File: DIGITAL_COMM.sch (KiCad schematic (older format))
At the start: 4 parts, among them U5 MCP3004, U6 TC77

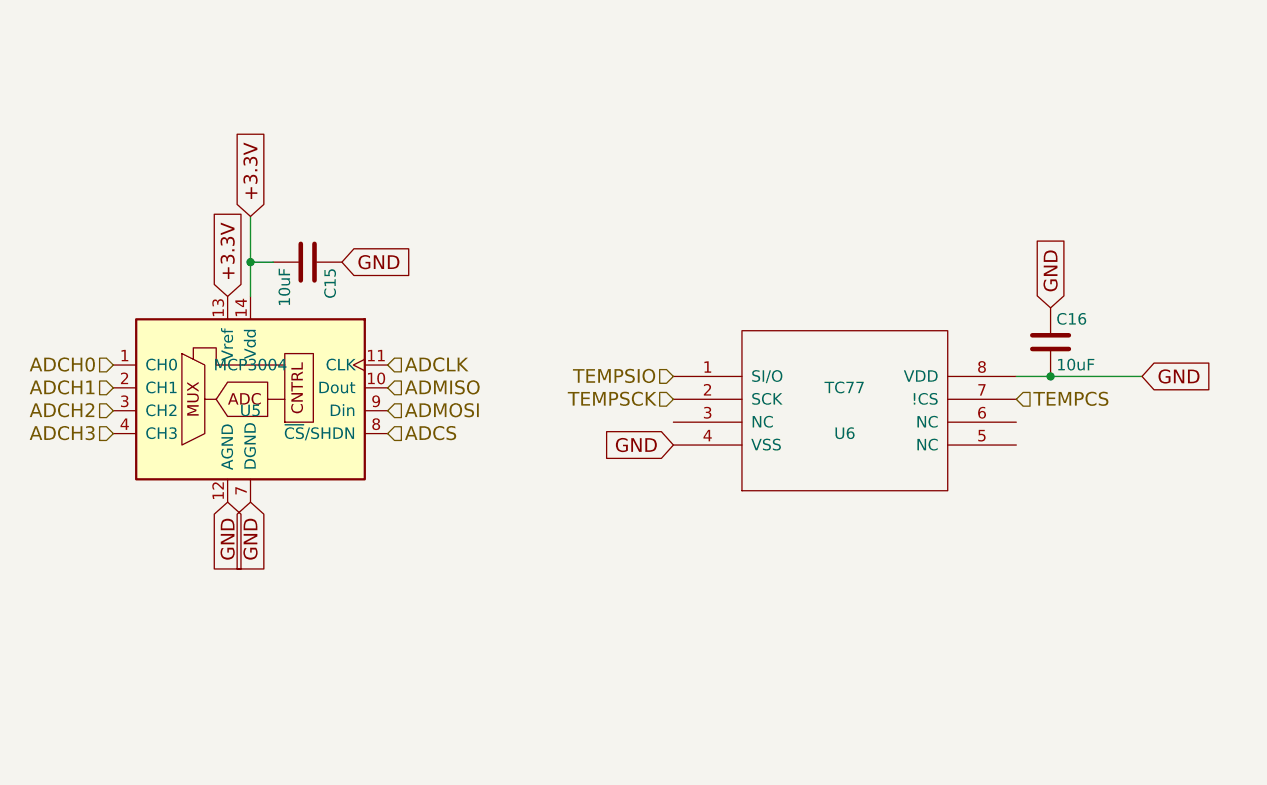
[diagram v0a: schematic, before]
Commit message: all components verified, pcb design required
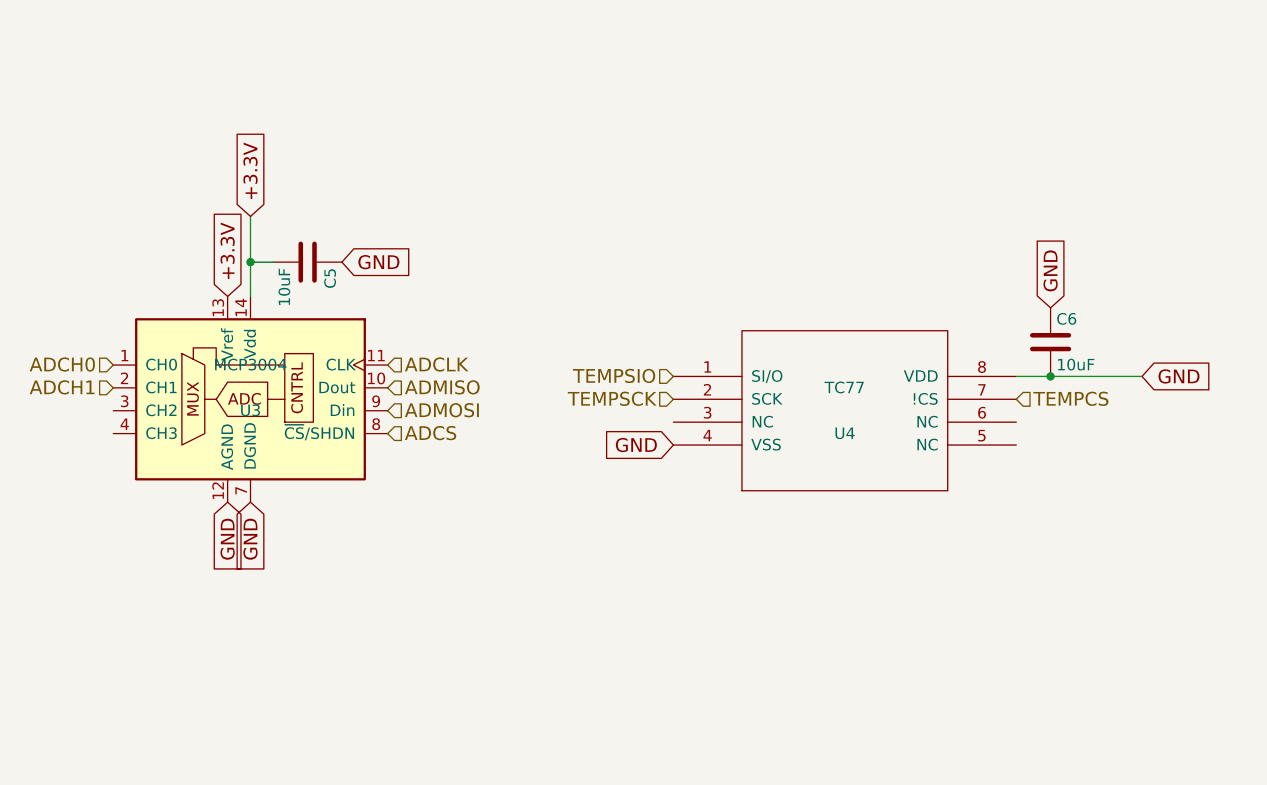
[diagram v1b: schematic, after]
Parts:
- renumbered C15 to C5, C16 to C6, U5 to U3, U6 to U4
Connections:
- net ADCH2: no longer names the net of U3.3 (CH2)
- net ADCH3: no longer names the net of U3.4 (CH3)
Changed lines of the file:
@@
 $EndDescr
 $Comp
-L MCP3004 U5
+L MCP3004 U3
 U 1 1 561B93E7
 P 3550 2600
-F 0 "U5" H 3550 2500 50  0000 C CNN
+F 0 "U3" H 3550 2500 50  0000 C CNN
 F 1 "MCP3004" H 3550 2700 50  0000 C CNN
 F 2 "Housings_SOIC:SOIC-14_3.9x8.7mm_Pitch1.27mm" H 3550 2600 50  0001 C CNN
@@
 $EndComp
 $Comp
-L TC77 U6
+L TC77 U4
 U 1 1 561B943C
 P 6150 2700
-F 0 "U6" H 6150 2600 50  0000 C CNN
+F 0 "U4" H 6150 2600 50  0000 C CNN
 F 1 "TC77" H 6150 2800 50  0000 C CNN
 F 2 "Housings_SOIC:SOIC-8_3.9x4.9mm_Pitch1.27mm" H 6150 2700 50  0001 C CNN
@@
 $EndComp
 $Comp
-L C C16
+L C C6
 U 1 1 561C1F39
 P 7050 2400
-F 0 "C16" H 7075 2500 50  0000 L CNN
+F 0 "C6" H 7075 2500 50  0000 L CNN
 F 1 "10uF" H 7075 2300 50  0000 L CNN
 F 2 "Capacitors_SMD:C_1206_HandSoldering" H 7088 2250 30  0001 C CNN
@@
 $EndComp
 $Comp
-L C C15
+L C C5
 U 1 1 561C1FA8
 P 3800 2050
-F 0 "C15" H 3825 2150 50  0000 L CNN
+F 0 "C5" H 3825 2150 50  0000 L CNN
 F 1 "10uF" H 3825 1950 50  0000 L CNN
 F 2 "Capacitors_SMD:C_1206_HandSoldering" H 3838 1900 30  0001 C CNN
@@
 	6900 2550 7450 2550
 Connection ~ 7050 2550
-Text HLabel 2950 2700 0    60   Input ~ 0
-ADCH2
-Text HLabel 2950 2800 0    60   Input ~ 0
-ADCH3
 Text GLabel 3550 1850 1    60   Input ~ 0
 +3.3V

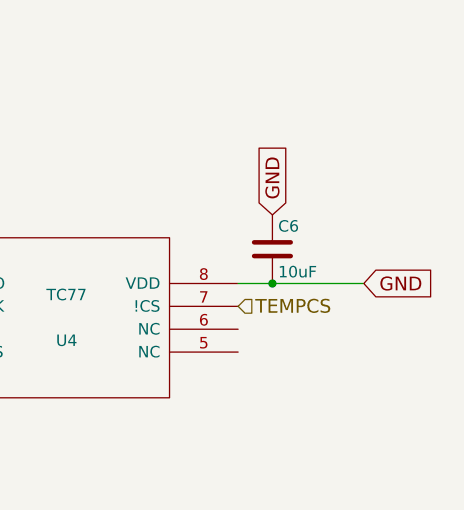
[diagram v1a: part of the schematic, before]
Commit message: backup before rewiring.
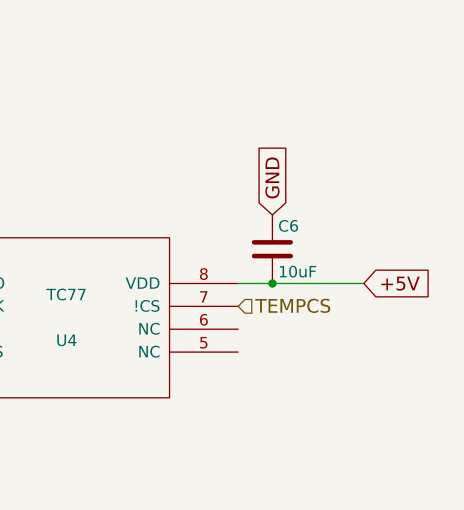
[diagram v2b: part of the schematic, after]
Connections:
- net GND: no longer C6.2, U4.8 (VDD)
- new net +5V: C6.2, U4.8 (VDD)
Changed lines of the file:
@@
 F 1 "TC77" H 6150 2800 50  0000 C CNN
 F 2 "Housings_SOIC:SOIC-8_3.9x4.9mm_Pitch1.27mm" H 6150 2700 50  0001 C CNN
-F 3 "http://www.mouser.com/http://www.mouser.com/ds/2/268/20092a-72501.pdfds/2/268/20092a-72501.pdf" H 6150 2700 50  0001 C CNN
+F 3 "http://ww1.microchip.com/downloads/en/devicedoc/20092a.pdf" H 6150 2700 50  0001 C CNN
 	1    6150 2700
 	1    0    0    -1
@@
 GND
 Text GLabel 7450 2550 2    60   Input ~ 0
-GND
++5V
 $EndSCHEMATC

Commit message: fixed links to the webpage of parts
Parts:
- U3: link (none) -> http://hu.farnell.com/microchip/mcp3004-i-sl/adc-10bit-2-7v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
- U4: link (none) -> http://hu.farnell.com/microchip/tc77-3-3moa/sensor-thermal-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
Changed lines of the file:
@@
 F 2 "Housings_SOIC:SOIC-14_3.9x8.7mm_Pitch1.27mm" H 3550 2600 50  0001 C CNN
 F 3 "http://ww1.microchip.com/downloads/en/DeviceDoc/21295C.pdf" H 3550 2600 50  0001 C CNN
+F 4 "http://hu.farnell.com/microchip/mcp3004-i-sl/adc-10bit-2-7v-4ch-spi-14soic/dp/1852016" H 3550 2600 60  0001 C CNN "link"
 	1    3550 2600
 	1    0    0    -1
@@
 F 2 "Housings_SOIC:SOIC-8_3.9x4.9mm_Pitch1.27mm" H 6150 2700 50  0001 C CNN
 F 3 "http://ww1.microchip.com/downloads/en/devicedoc/20092a.pdf" H 6150 2700 50  0001 C CNN
+F 4 "http://hu.farnell.com/microchip/tc77-3-3moa/sensor-thermal-13bit-spitm-smd/dp/1439513" H 6150 2700 60  0001 C CNN "link"
 	1    6150 2700
 	1    0    0    -1

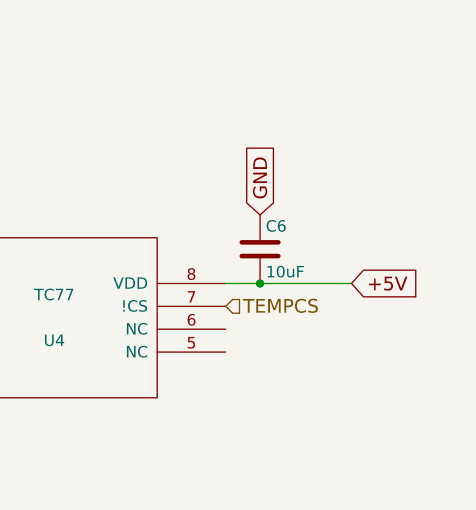
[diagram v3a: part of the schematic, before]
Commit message: parts corrected after review; dc/dc converter has to be ordered
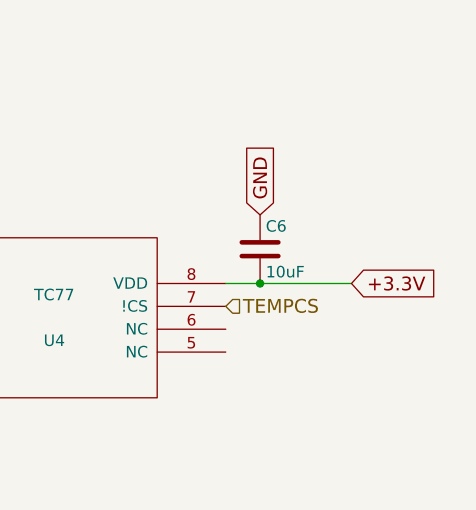
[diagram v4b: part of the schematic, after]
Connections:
- net +5V is gone; now on net +3.3V: C6.2, U4.8 (VDD)
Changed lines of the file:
@@
 GND
 Text GLabel 7450 2550 2    60   Input ~ 0
-+5V
++3.3V
 $EndSCHEMATC

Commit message: before wiring
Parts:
- renumbered C5 to C7, C6 to C8, U3 to U4, U4 to U5
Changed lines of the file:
@@
 $EndDescr
 $Comp
-L MCP3004 U3
+L MCP3004 U4
 U 1 1 561B93E7
 P 3550 2600
-F 0 "U3" H 3550 2500 50  0000 C CNN
+F 0 "U4" H 3550 2500 50  0000 C CNN
 F 1 "MCP3004" H 3550 2700 50  0000 C CNN
 F 2 "Housings_SOIC:SOIC-14_3.9x8.7mm_Pitch1.27mm" H 3550 2600 50  0001 C CNN
@@
 $EndComp
 $Comp
-L TC77 U4
+L TC77 U5
 U 1 1 561B943C
 P 6150 2700
-F 0 "U4" H 6150 2600 50  0000 C CNN
+F 0 "U5" H 6150 2600 50  0000 C CNN
 F 1 "TC77" H 6150 2800 50  0000 C CNN
 F 2 "Housings_SOIC:SOIC-8_3.9x4.9mm_Pitch1.27mm" H 6150 2700 50  0001 C CNN
@@
 $EndComp
 $Comp
-L C C6
+L C C8
 U 1 1 561C1F39
 P 7050 2400
-F 0 "C6" H 7075 2500 50  0000 L CNN
+F 0 "C8" H 7075 2500 50  0000 L CNN
 F 1 "10uF" H 7075 2300 50  0000 L CNN
 F 2 "Capacitors_SMD:C_1206_HandSoldering" H 7088 2250 30  0001 C CNN
@@
 $EndComp
 $Comp
-L C C5
+L C C7
 U 1 1 561C1FA8
 P 3800 2050
-F 0 "C5" H 3825 2150 50  0000 L CNN
+F 0 "C7" H 3825 2150 50  0000 L CNN
 F 1 "10uF" H 3825 1950 50  0000 L CNN
 F 2 "Capacitors_SMD:C_1206_HandSoldering" H 3838 1900 30  0001 C CNN

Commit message: before new pcb; - the order of the gpio pins have changed in accordance with olinuxino - indicator leds have been added for debugging - ad current pin added for debugging
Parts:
- U4: link http://hu.farnell.com/microchip/mcp3004-i-sl/adc-10bit-2-7v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 -> (none); pdf (none) -> http://ww1.microchip.com/downloads/en/DeviceDoc/21295C.pdf
- U5: link http://hu.farnell.com/microchip/tc77-3-3moa/sensor-thermal-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 -> (none); pdf (none) -> http://ww1.microchip.com/downloads/en/devicedoc/20092a.pdf
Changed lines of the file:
@@
 F 1 "MCP3004" H 3550 2700 50  0000 C CNN
 F 2 "Housings_SOIC:SOIC-14_3.9x8.7mm_Pitch1.27mm" H 3550 2600 50  0001 C CNN
-F 3 "http://ww1.microchip.com/downloads/en/DeviceDoc/21295C.pdf" H 3550 2600 50  0001 C CNN
-F 4 "http://hu.farnell.com/microchip/mcp3004-i-sl/adc-10bit-2-7v-4ch-spi-14soic/dp/1852016" H 3550 2600 60  0001 C CNN "link"
+F 3 "http://hu.farnell.com/microchip/mcp3004-i-sl/adc-10bit-2-7v-4ch-spi-14soic/dp/1852016" H 3550 2600 50  0001 C CNN
+F 4 "http://ww1.microchip.com/downloads/en/DeviceDoc/21295C.pdf" H 3550 2600 60  0001 C CNN "pdf"
 	1    3550 2600
 	1    0    0    -1
@@
 F 1 "TC77" H 6150 2800 50  0000 C CNN
 F 2 "Housings_SOIC:SOIC-8_3.9x4.9mm_Pitch1.27mm" H 6150 2700 50  0001 C CNN
-F 3 "http://ww1.microchip.com/downloads/en/devicedoc/20092a.pdf" H 6150 2700 50  0001 C CNN
-F 4 "http://hu.farnell.com/microchip/tc77-3-3moa/sensor-thermal-13bit-spitm-smd/dp/1439513" H 6150 2700 60  0001 C CNN "link"
+F 3 "http://hu.farnell.com/microchip/tc77-3-3moa/sensor-thermal-13bit-spitm-smd/dp/1439513" H 6150 2700 50  0001 C CNN
+F 4 "http://ww1.microchip.com/downloads/en/devicedoc/20092a.pdf" H 6150 2700 60  0001 C CNN "pdf"
 	1    6150 2700
 	1    0    0    -1
@@
 Text HLabel 2950 2600 0    60   Input ~ 0
 ADCH1
-Wire Wire Line
-	6900 2550 7450 2550
-Connection ~ 7050 2550
 Text GLabel 3550 1850 1    60   Input ~ 0
 +3.3V
-Wire Wire Line
-	3550 1850 3550 2200
-Wire Wire Line
-	3550 2050 3650 2050
 Text GLabel 3950 2050 2    60   Input ~ 0
 GND
-Connection ~ 3550 2050
 Text GLabel 3450 2200 1    60   Input ~ 0
 +3.3V
@@
 Text GLabel 7450 2550 2    60   Input ~ 0
 +3.3V
+Wire Wire Line
+	6900 2550 7450 2550
+Connection ~ 7050 2550
+Wire Wire Line
+	3550 1850 3550 2200
+Wire Wire Line
+	3550 2050 3650 2050
+Connection ~ 3550 2050
 $EndSCHEMATC

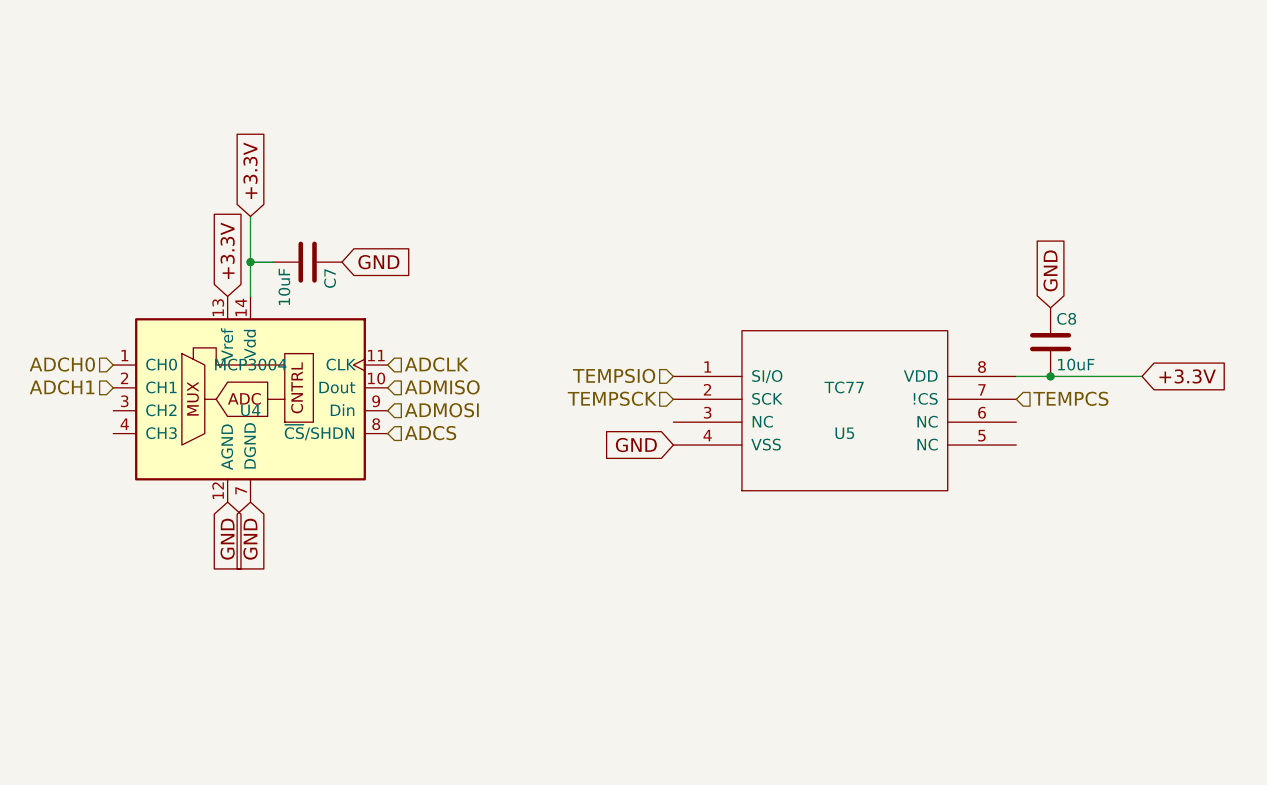
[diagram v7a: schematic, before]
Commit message: Analog grounds and filtered reference voltage for the DAC.
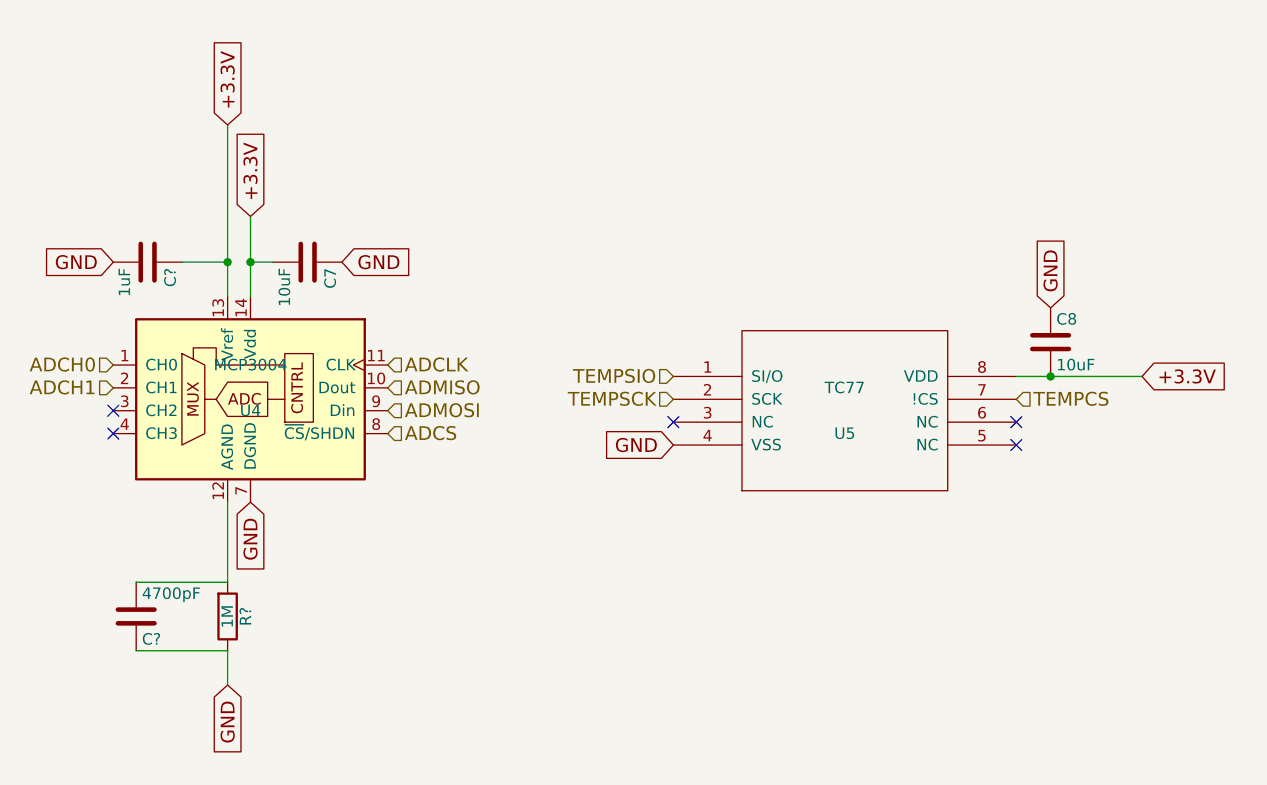
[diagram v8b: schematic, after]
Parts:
- added C?: 4700pF, symbol C
- added C?: 1uF, symbol C
- added R?: 1M, symbol R
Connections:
- net +3.3V: now also C?.1
- net GND: now also C?.1, C?.2, R?.1; no longer U4.12 (AGND)
- new net: C?.2, R?.2, U4.12 (AGND)
- no-connect marks 0 -> 5
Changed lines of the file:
@@
 Text GLabel 3950 2050 2    60   Input ~ 0
 GND
-Text GLabel 3450 2200 1    60   Input ~ 0
+Text GLabel 3450 1450 1    60   Input ~ 0
 +3.3V
 Text GLabel 3550 3100 3    60   Input ~ 0
-GND
-Text GLabel 3450 3100 3    60   Input ~ 0
 GND
 Text GLabel 7050 2250 1    60   Input ~ 0
@@
 	3550 2050 3650 2050
 Connection ~ 3550 2050
+Text GLabel 3450 3900 3    60   Input ~ 0
+GND
+$Comp
+L C C?
+U 1 1 59A60423
+P 3050 3600
+F 0 "C?" H 3075 3700 50  0000 L CNN
+F 1 "4700pF" H 3075 3500 50  0000 L CNN
+F 2 "" H 3088 3450 50  0001 C CNN
+F 3 "" H 3050 3600 50  0001 C CNN
+	1    3050 3600
+	1    0    0    1
+$EndComp
+$Comp
+L R R?
+U 1 1 59A6042A
+P 3450 3600
+F 0 "R?" V 3530 3600 50  0000 C CNN
+F 1 "1M" V 3450 3600 50  0000 C CNN
+F 2 "" V 3380 3600 50  0001 C CNN
+F 3 "" H 3450 3600 50  0001 C CNN
+	1    3450 3600
+	1    0    0    1
+$EndComp
+Wire Wire Line
+	3450 3900 3450 3750
+Wire Wire Line
+	3450 3750 3050 3750
+Wire Wire Line
+	3450 3450 3050 3450
+Wire Wire Line
+	3450 3100 3450 3450
+$Comp
+L C C?
+U 1 1 59A609F8
+P 3100 2050
+F 0 "C?" H 3125 2150 50  0000 L CNN
+F 1 "1uF" H 3125 1950 50  0000 L CNN
+F 2 "" H 3138 1900 50  0001 C CNN
+F 3 "" H 3100 2050 50  0001 C CNN
+	1    3100 2050
+	0    1    1    0
+$EndComp
+Wire Wire Line
+	3450 2200 3450 1450
+Wire Wire Line
+	3250 2050 3450 2050
+Connection ~ 3450 2050
+Text GLabel 2950 2050 0    60   Input ~ 0
+GND
+NoConn ~ 6900 2750
+NoConn ~ 6900 2850
+NoConn ~ 5400 2750
+NoConn ~ 2950 2800
+NoConn ~ 2950 2700
 $EndSCHEMATC
